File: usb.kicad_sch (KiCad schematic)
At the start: 23 parts, among them J4 CONN_02X03, U1 LFE5U-85F-6BG381C, U6 FT231XS, Y1 FNETHE025

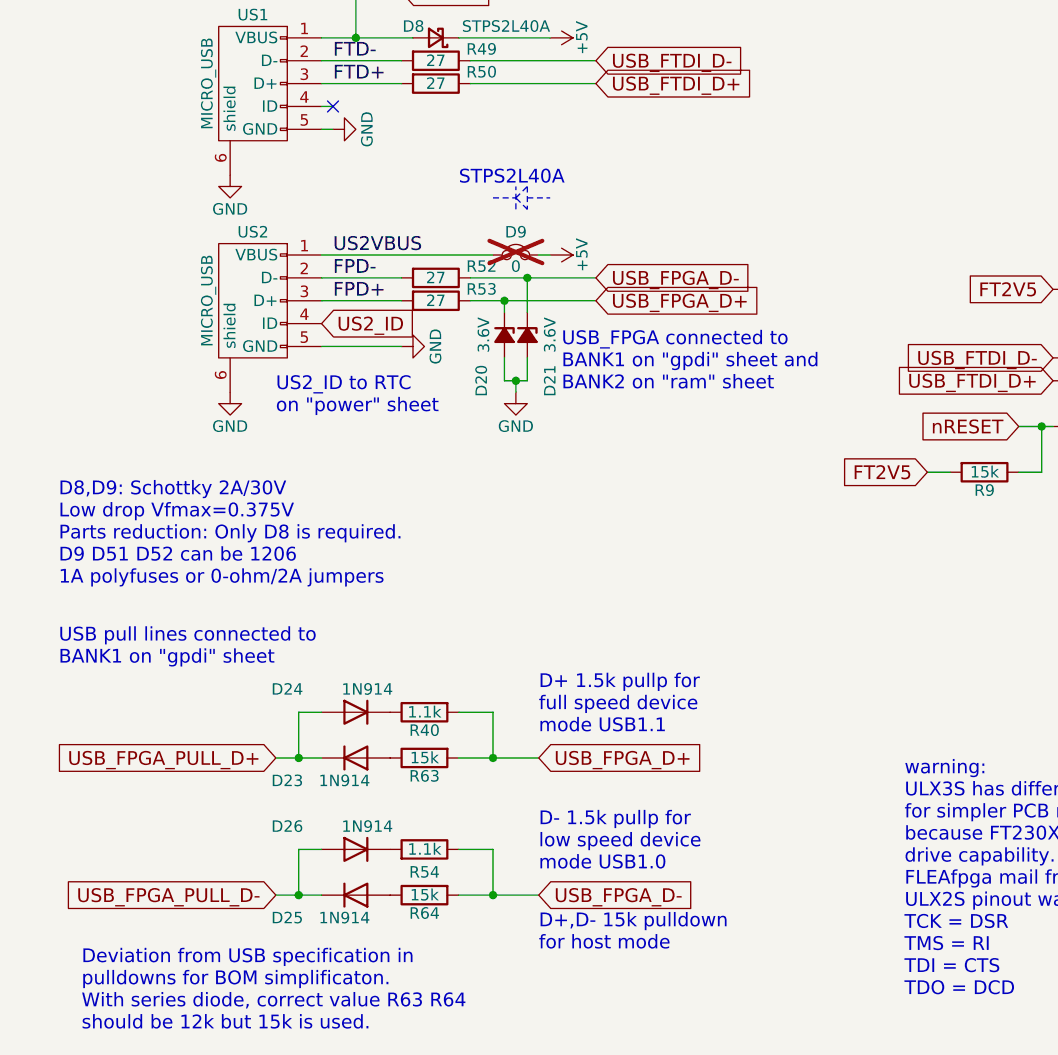
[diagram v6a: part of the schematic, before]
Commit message: remove US2 port
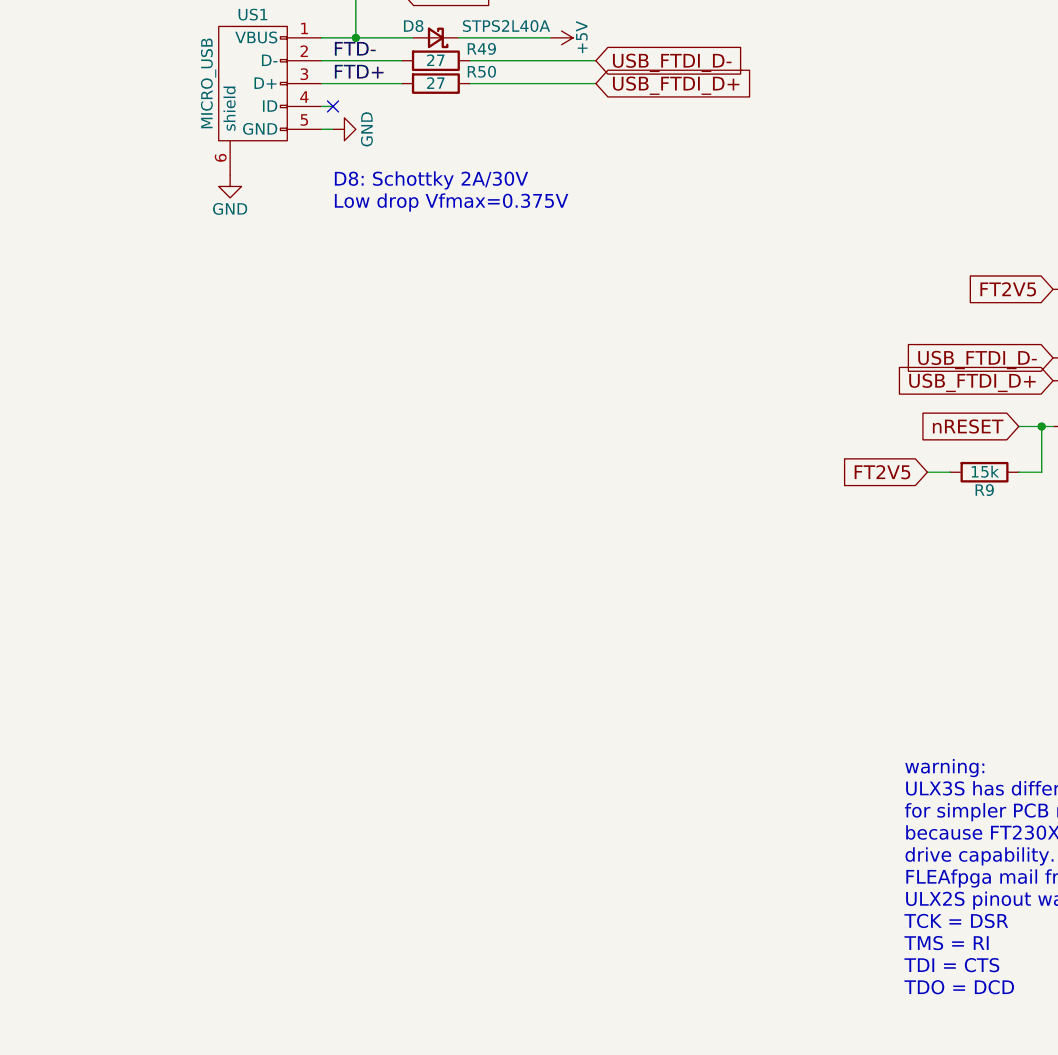
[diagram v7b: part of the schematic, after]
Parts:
- removed D20, D21: 3.6V, Diode_SMD:D_SOD-323_HandSoldering, symbol Device:D_Zener_Small_ALT
- removed D23, D24, D25, D26: 1N914, Diode_SMD:D_SOD-323_HandSoldering, symbol Device:D
- removed D9: 0, jumper:D_SMA_Jumper_NC, symbol Device:Jumper_NC_Small
- removed R40, R54: 1.1k, Resistor_SMD:R_0603_1608Metric, symbol Device:R
- removed R52, R53: 27, Resistor_SMD:R_0603_1608Metric, symbol Device:R
- removed R63, R64: 15k, Resistor_SMD:R_0603_1608Metric, symbol Device:R
- removed US2: MICRO_USB, usb_otg:USB-MICRO-B-FCI-10118192-0001LF, symbol ulx3s-rescue:USB_OTG
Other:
- note added: "D8: Schottky 2A/30V Low drop Vfmax=0.375V"
- note removed: "D+ 1.5k pullp for full speed device mode USB1.1"
- note removed: "D+,D- 15k pulldown for host mode"
- note removed: "D- 1.5k pullp for low speed device mode USB1.0"
- note removed: "D8,D9: Schottky 2A/30V Low drop Vfmax=0.375V Parts reduction: Only D8 is required. D9 D51 D52 can be 1206 1A polyfuses or 0-ohm/2A jumpers"
- note removed: "Deviation from USB specification in pulldowns for BOM simplificaton. With series diode, correct value R63 R64 should be 12k but 15k is used."
- note removed: "STPS2L40A"
- note removed: "US2_ID to RTC on "power" sheet"
- note removed: "USB pull lines connected to BANK1 on "gpdi" sheet"
- note removed: "USB_FPGA connected to BANK1 on "gpdi" sheet and BANK2 on "ram" sheet"

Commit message: switch to new oscillator
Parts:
- Y1: value FNETHE025 -> ECS-1612MV-250-CN-TR; footprint oscxo:Crystal_SMD_7050_4Pads -> ecs1612mv:OSC_ECS-1612MV-250-CN-TR-4; Digike_y1 FNETHE025CT-ND -> (none); Digikey 3305-7050XOM2500BMD13CCC-CT-ND -> XC2830CT-ND; Koncar FQ001 -> (none); LCSC C390569 -> C405444; MNF1_URL www.diodes.com -> ecsxtal.com; MNF3_URL https://datasheet.lcsc.com/szlcsc/1912111437_Shenzhen-SCTF-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 -> (none); MPN FNETHE025 -> 520-1612MV-250-CNT; MPN2 SiT8008BC-81-33E-25.000000X -> (none); MPN3 S7D25.000000D20F30T -> (none); Mouse_r2 788-8008BC8133E25X -> (none); Mouser 729-FNETHE025 -> (none); Newark 80AC8624 -> 57AK3015; Side T -> (none); price100_Digikey 0.7942$ -> (none)
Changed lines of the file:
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@@
 			)
 		)
-		(property "Value" "FNETHE025"
+		(property "Value" "ECS-1612MV-250-CN-TR"
 			(at 141.732 39.624 0)
 			(show_name no)
@@
 			)
 		)
-		(property "Footprint" "oscxo:Crystal_SMD_7050_4Pads"
+		(property "Footprint" "ecs1612mv:OSC_ECS-1612MV-250-CN-TR-4"
 			(at 138.43 36.83 0)
 			(hide yes)
@@
 			)
 		)
-		(property "Datasheet" ""
+		(property "Datasheet" "https://ecsxtal.com/store/pdf/ECS-1612MV.pdf"
 			(at 138.43 36.83 0)
 			(hide yes)
@@
 			)
 		)
-		(property "Description" "Four pin crystal, GND on pins 2 and 4"
+		(property "Description" "Four pin crystal"
 			(at 138.43 36.83 0)
 			(hide yes)
@@
 			)
 		)
-		(property "MNF1_URL" "www.diodes.com"
+		(property "MNF1_URL" "ecsxtal.com"
 			(at 138.43 36.83 0)
 			(hide yes)
@@
 			)
 		)
-		(property "MPN" "FNETHE025"
+		(property "MPN" "520-1612MV-250-CNT"
 			(at 138.43 36.83 0)
 			(hide yes)
@@
 			)
 		)
-		(property "MPN2" "SiT8008BC-81-33E-25.000000X"
+		(property "Digikey" "XC2830CT-ND"
 			(at 138.43 36.83 0)
 			(hide yes)
@@
 			)
 		)
-		(property "MNF3_URL" "https://datasheet.lcsc.com/szlcsc/1912111437_Shenzhen-SCTF-Elec-S7D25-000000D20F30T_C387026.pdf"
+		(property "Newark" "57AK3015"
 			(at 138.43 36.83 0)
 			(hide yes)
@@
 			)
 		)
-		(property "MPN3" "S7D25.000000D20F30T"
+		(property "LCSC" "C405444"
 			(at 138.43 36.83 0)
 			(hide yes)
@@
 				)
 			)
-		)
-		(property "Mouser" "729-FNETHE025"
-			(at 138.43 36.83 0)
-			(hide yes)
-			(show_name no)
-			(do_not_autoplace no)
-			(effects
-				(font
-					(size 1.524 1.524)
-				)
-			)
-		)
-		(property "Mouse_r2" "788-8008BC8133E25X "
-			(at 138.43 36.83 0)
-			(hide yes)
-			(show_name no)
-			(do_not_autoplace no)
-			(effects
-				(font
-					(size 1.27 1.27)
-				)
-			)
-		)
-		(property "Digikey" "3305-7050XOM2500BMD13CCC-CT-ND"
-			(at 138.43 36.83 0)
-			(hide yes)
-			(show_name no)
-			(do_not_autoplace no)
-			(effects
-				(font
-					(size 1.27 1.27)
-				)
-			)
-		)
-		(property "Digike_y1" "FNETHE025CT-ND"
-			(at 138.43 36.83 0)
-			(hide yes)
-			(show_name no)
-			(do_not_autoplace no)
-			(effects
-				(font
-					(size 1.27 1.27)
-				)
-			)
-		)
-		(property "Newark" "80AC8624"
-			(at 138.43 36.83 0)
-			(hide yes)
-			(show_name no)
-			(do_not_autoplace no)
-			(effects
-				(font
-					(size 1.27 1.27)
-				)
-			)
-		)
-		(property "LCSC" "C390569"
-			(at 138.43 36.83 0)
-			(hide yes)
-			(show_name no)
-			(do_not_autoplace no)
-			(effects
-				(font
-					(size 1.27 1.27)
-				)
-			)
-		)
-		(property "price100_Digikey" "0.7942$"
-			(at 138.43 36.83 0)
-			(hide yes)
-			(show_name no)
-			(do_not_autoplace no)
-			(effects
-				(font
-					(size 1.27 1.27)
-				)
-			)
-		)
-		(property "Koncar" "FQ001"
-			(at 138.43 36.83 0)
-			(hide yes)
-			(show_name no)
-			(do_not_autoplace no)
-			(effects
-				(font
-					(size 1.27 1.27)
-				)
-			)
-		)
-		(property "Side" "T"
-			(at 138.43 36.83 0)
-			(hide yes)
-			(show_name no)
-			(do_not_autoplace no)
-			(effects
-				(font
-					(size 1.27 1.27)
-				)
-			)
-		)
-		(property "Arrow" ""
-			(at 138.43 36.83 0)
-			(hide yes)
-			(show_name no)
-			(do_not_autoplace no)
-			(effects
-				(font
-					(size 1.524 1.524)
-				)
-			)
-		)
-		(property "DatasheetLC" ""
-			(at 138.43 36.83 0)
-			(hide yes)
-			(show_name no)
-			(do_not_autoplace no)
-			(effects
-				(font
-					(size 1.524 1.524)
-				)
-			)
-		)
-		(property "LCS_C2" ""
-			(at 138.43 36.83 0)
-			(hide yes)
-			(show_name no)
-			(do_not_autoplace no)
-			(effects
-				(font
-					(size 1.524 1.524)
-				)
-			)
-		)
-		(property "MP_N4" ""
-			(at 138.43 36.83 0)
-			(hide yes)
-			(show_name no)
-			(do_not_autoplace no)
-			(effects
-				(font
-					(size 1.524 1.524)
-				)
-			)
-		)
-		(property "MP_N5" ""
-			(at 138.43 36.83 0)
-			(hide yes)
-			(show_name no)
-			(do_not_autoplace no)
-			(effects
-				(font
-					(size 1.524 1.524)
-				)
-			)
-		)
-		(property "Vertical" ""
-			(at 138.43 36.83 0)
-			(hide yes)
-			(show_name no)
-			(do_not_autoplace no)
-			(effects
-				(font
-					(size 1.524 1.524)
-				)
-			)
-		)
-		(property "price100_Mouser" ""
-			(at 138.43 36.83 0)
-			(hide yes)
-			(show_name no)
-			(do_not_autoplace no)
-			(effects
-				(font
-					(size 1.524 1.524)
-				)
-			)
-		)
-		(property "price1200_Chip1stop" ""
-			(at 138.43 36.83 0)
-			(hide yes)
-			(show_name no)
-			(do_not_autoplace no)
-			(effects
-				(font
-					(size 1.524 1.524)
-				)
-			)
-		)
-		(property "price300_LCSC" ""
-			(at 138.43 36.83 0)
-			(hide yes)
-			(show_name no)
-			(do_not_autoplace no)
-			(effects
-				(font
-					(size 1.524 1.524)
-				)
-			)
-		)
-		(property "price300_Vertical" ""
-			(at 138.43 36.83 0)
-			(hide yes)
-			(show_name no)
-			(do_not_autoplace no)
-			(effects
-				(font
-					(size 1.524 1.524)
-				)
-			)
-		)
-		(property "price_Arrow" ""
-			(at 138.43 36.83 0)
-			(hide yes)
-			(show_name no)
-			(do_not_autoplace no)
-			(effects
-				(font
-					(size 1.524 1.524)
-				)
-			)
